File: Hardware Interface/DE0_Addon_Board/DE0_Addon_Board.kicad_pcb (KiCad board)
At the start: 2 copper layers, 27.7 x 56.6 mm, 5 parts, among them J1 Conn_02x20_Odd_Even, J2 Conn_01x05_Male, U1 IS61WV25616EDBLL

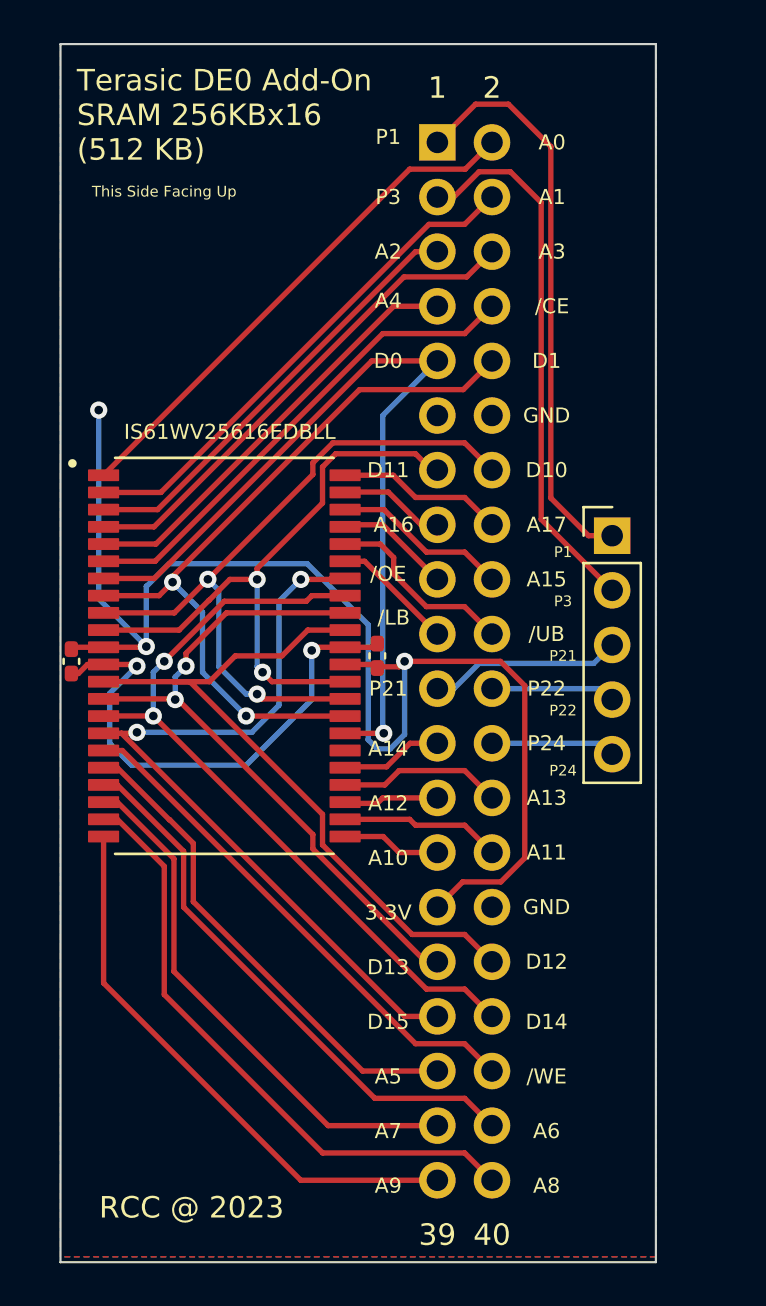
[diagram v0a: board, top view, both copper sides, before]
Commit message: Added 2nd IDC connector in paralell with the SRAM
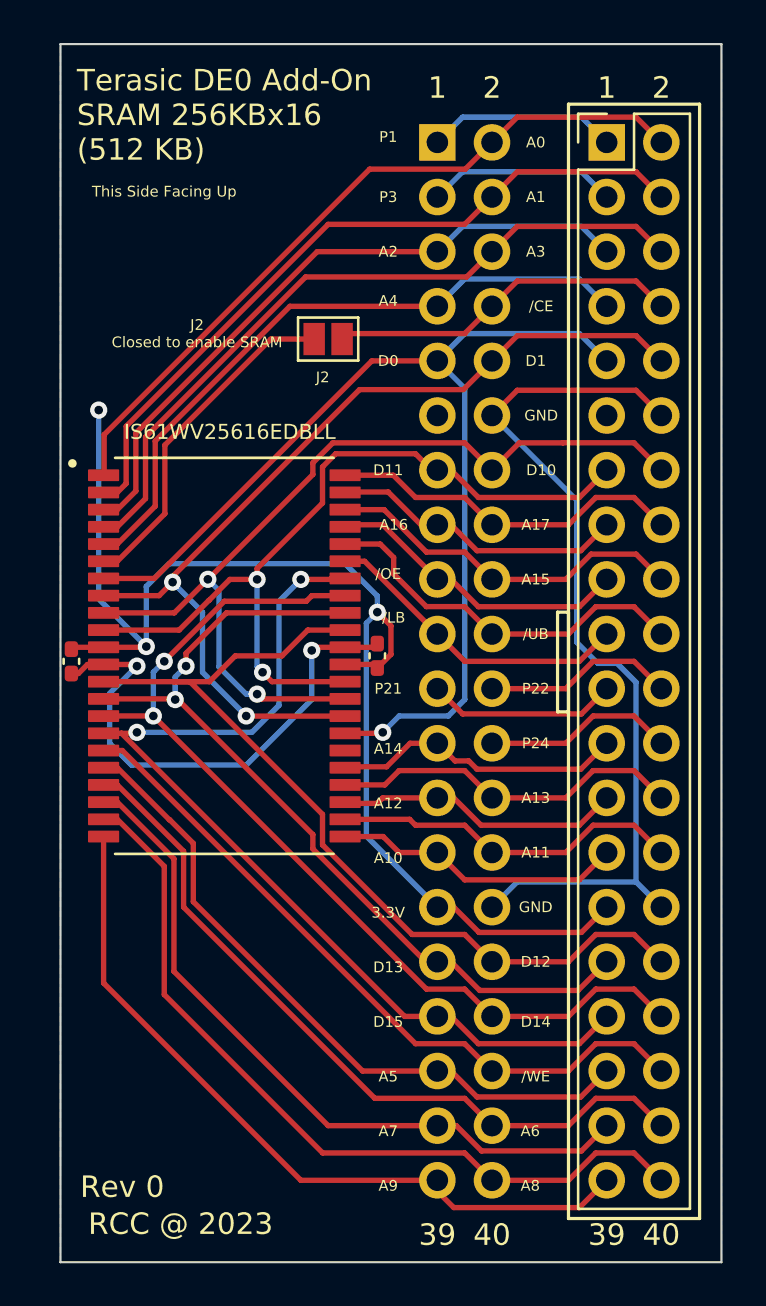
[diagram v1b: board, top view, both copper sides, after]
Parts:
- added J3: Conn_02x20_Odd_Even, Connector_PinHeader_2.54mm:PinHeader_2x20_P2.54mm_Vertical, F.Cu at (63.2, 26.4)
- J2: value Conn_01x05_Male -> Conn_01x02_Male; footprint Connector_PinHeader_2.54mm:PinHeader_1x05_P2.54mm_Vertical -> Jumper:SolderJumper-2_P1.3mm_Open_Pad1.0x1.5mm
- moved J2 16.1 mm to (50.3, 35.6)
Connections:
- J2 pad 1: P1 -> MEM_CE_n
- J2 pad 2: P3 -> CE_n
- U1 pad 6: CE_n -> MEM_CE_n
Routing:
- net GNDREF: track 23.7 -> 66.4 mm
- net P1: track 26.7 -> 8.85 mm
- net P3: track 25.3 -> 8.85 mm
- net MEM_CE_n: track 0.00 -> 15.9 mm
- net D0: track 39.9 -> 51.1 mm
- net A4: track 20.1 -> 30.8 mm
- net A3: track 23.4 -> 33.9 mm
- net A2: track 20.5 -> 30.9 mm
- net A1: track 23.8 -> 34.2 mm
- net A0: track 24.5 -> 34.4 mm
- net A9: track 26.1 -> 35.4 mm
- net D13: track 31.5 -> 40.5 mm
- net D10: track 32.9 -> 41.9 mm
- net WE_n: track 24.2 -> 33.2 mm
- net UB_n: track 9.01 -> 17.9 mm
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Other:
- board size 27.7 x 56.6 mm -> 30.7 x 56.6 mm
- board text added: "J2 Closed to enable SRAM"
- board text added: "Rev 0"

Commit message: Changed footprint of SRAM decoupling capacitors to SMD 0603; Updated SRAM Addon for Rev.2
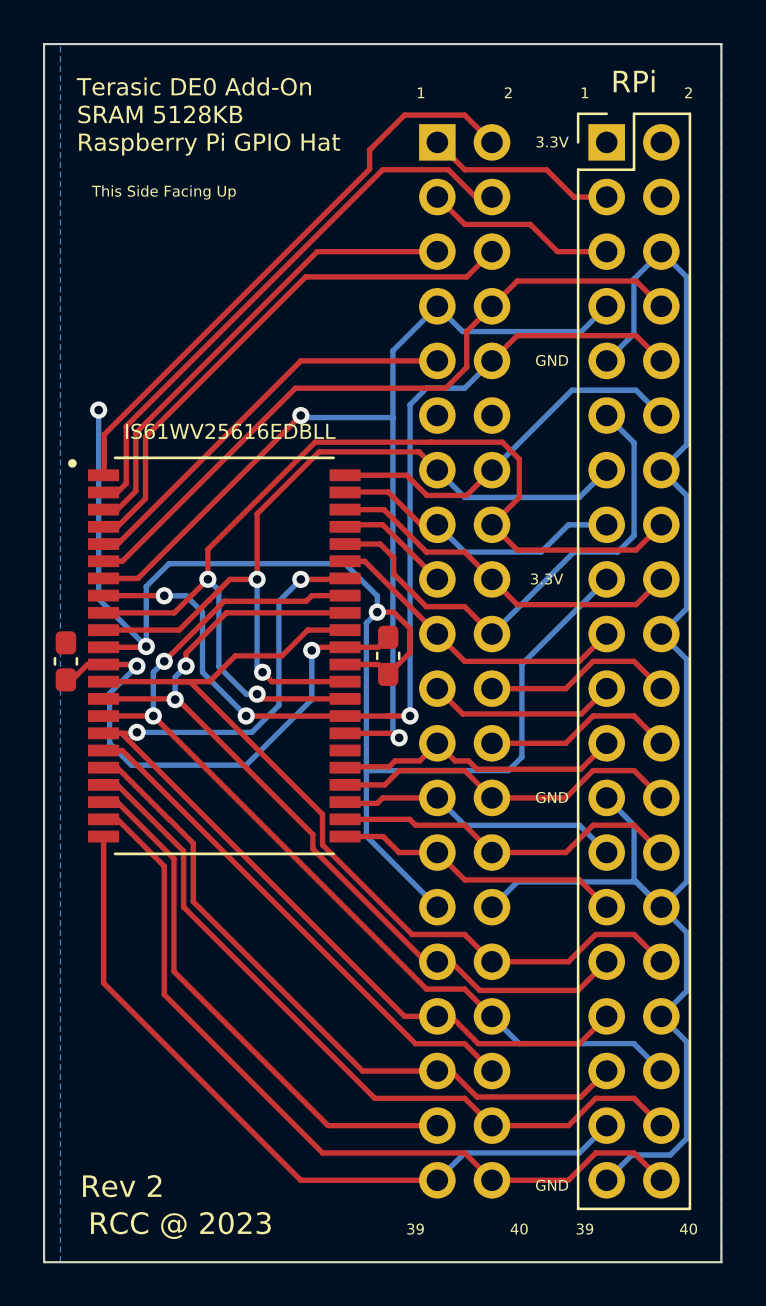
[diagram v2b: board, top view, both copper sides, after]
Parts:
- removed J2: Conn_01x02_Male, Jumper:SolderJumper-2_P1.3mm_Open_Pad1.0x1.5mm
- C1, C2: footprint Capacitor_SMD:C_0402_1005Metric_Pad0.74x0.62mm_HandSolder -> Capacitor_SMD:C_0603_1608Metric_Pad1.08x0.95mm_HandSolder
- J1: value Conn_02x20_Odd_Even -> DE0/DE1 IDC Connector
- J3: value Conn_02x20_Odd_Even -> Raspberry Pi Pin Header
- moved C1 0.51 mm to (53.1, 50.3)
- moved C2 0.25 mm to (38.1, 50.5)
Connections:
- net LB_n renamed IORQ_n
- net P22 renamed M1_n
- net P24 renamed INT_n
- J1 pad 14: D10 -> A17
- J1 pad 16: A17 -> D10
- J1 pad 20: UB_n -> RESET_n
- J1 pad 36: WE_n -> P36
- J1 pad 7: A4 -> D0
- J1 pad 8: CE_n -> BUSDIR_n
- J1 pad 9: D0 -> A4
- J3 pad 1: P1 -> +3.3V
- J3 pad 11: unconnected-(J3-Pad11) -> RESET_n
- J3 pad 12: GNDREF -> A17
- J3 pad 14: D10 -> GNDREF
- J3 pad 16: A17 -> D10
- J3 pad 17: OE_n -> +3.3V
- J3 pad 2: A0 -> unconnected-(J3-Pad2)
- J3 pad 20: UB_n -> GNDREF
- J3 pad 25: A12 -> GNDREF
- J3 pad 27: A10 -> A12
- J3 pad 29: +3.3V -> A10
- J3 pad 3: P3 -> P1
- J3 pad 34: D14 -> GNDREF
- J3 pad 36: WE_n -> D14
- J3 pad 37: A7 -> A9
- J3 pad 39: A9 -> GNDREF
- J3 pad 4: A1 -> unconnected-(J3-Pad4)
- J3 pad 5: A2 -> P3
- J3 pad 6: A3 -> GNDREF
- J3 pad 7: A4 -> D0
- J3 pad 8: CE_n -> BUSDIR_n
- J3 pad 9: D0 -> GNDREF
- U1 pad 17: WE_n -> P36
- U1 pad 40: UB_n -> RESET_n
- U1 pad 6: MEM_CE_n -> BUSDIR_n
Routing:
- net WE_n: track 33.2 -> 0.00 mm
- net BUSDIR_n: track 0.00 -> 32.8 mm
- net GNDREF: track 66.4 -> 96.2 mm
- net P36: track 0.00 -> 24.2 mm
- net RESET_n: track 0.00 -> 23.6 mm
- net UB_n: track 17.9 -> 0.00 mm
- net CE_n: track 16.4 -> 0.00 mm
- net MEM_CE_n: track 15.9 -> 0.00 mm
- net A4: track 30.8 -> 19.0 mm
- net +3.3V: track 59.6 -> 69.0 mm
- net OE_n: track 14.3 -> 5.38 mm
- net A7: track 33.7 -> 24.8 mm
- net A3: track 33.9 -> 25.0 mm
- net A2: track 30.9 -> 22.1 mm
- net A1: track 34.2 -> 26.4 mm
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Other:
- board size 30.7 x 56.6 mm -> 31.5 x 56.6 mm
- board text added: "DE0"
- board text added: "Install in DE0 GPIO 0 With This Side Facing Down"
- board text added: "RPi"
- board text added: "Rev 2"
- board text added: "Terasic DE0 Add-On SRAM 5128KB Raspberry Pi GPIO Hat"
- board text removed: "/CE"
- board text removed: "/LB"
- board text removed: "/OE"
- board text removed: "/UB"
- board text removed: "/WE"
- board text removed: "A0"
- board text removed: "A1"
- board text removed: "A10"
- board text removed: "A11"
- board text removed: "A12"
- board text removed: "A13"
- board text removed: "A14"
- board text removed: "A15"
- board text removed: "A16"
- board text removed: "A17"
- board text removed: "A2"
- board text removed: "A3"
- board text removed: "A4"
- board text removed: "A5"
- board text removed: "A6"
- board text removed: "A7"
- board text removed: "A8"
- board text removed: "A9"
- board text removed: "D0"
- board text removed: "D1"
- board text removed: "D10"
- board text removed: "D11"
- board text removed: "D12"
- board text removed: "D13"
- board text removed: "D14"
- board text removed: "D15"
- board text removed: "Install in DE0 JP1 With This Side Facing Down"
- board text removed: "J2 Closed to enable SRAM"
- board text removed: "Mount Female Conector In This Side"
- board text removed: "P1"
- board text removed: "P21"
- board text removed: "P22"
- board text removed: "P24"
- board text removed: "P3"
- board text removed: "Rev 0"
- board text removed: "Terasic DE0 Add-On SRAM 256KBx16 (512 KB)"
